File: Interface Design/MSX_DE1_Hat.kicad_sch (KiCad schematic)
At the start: 31 parts, among them J1 DE1 GPIO, J2 Conn_01x03_Male, J3 Conn_01x03_Male, J4 Conn_01x03_Male, J5 Conn_01x03_Male, J6 Conn_01x03_Male, J7 Conn_01x03_Male, J8 Conn_01x03_Male, U1 74LVC245A, U2 74LVC245A, U3 74LVC245A, U4 74LVC245A, U5 74LVC245A, U6 4077

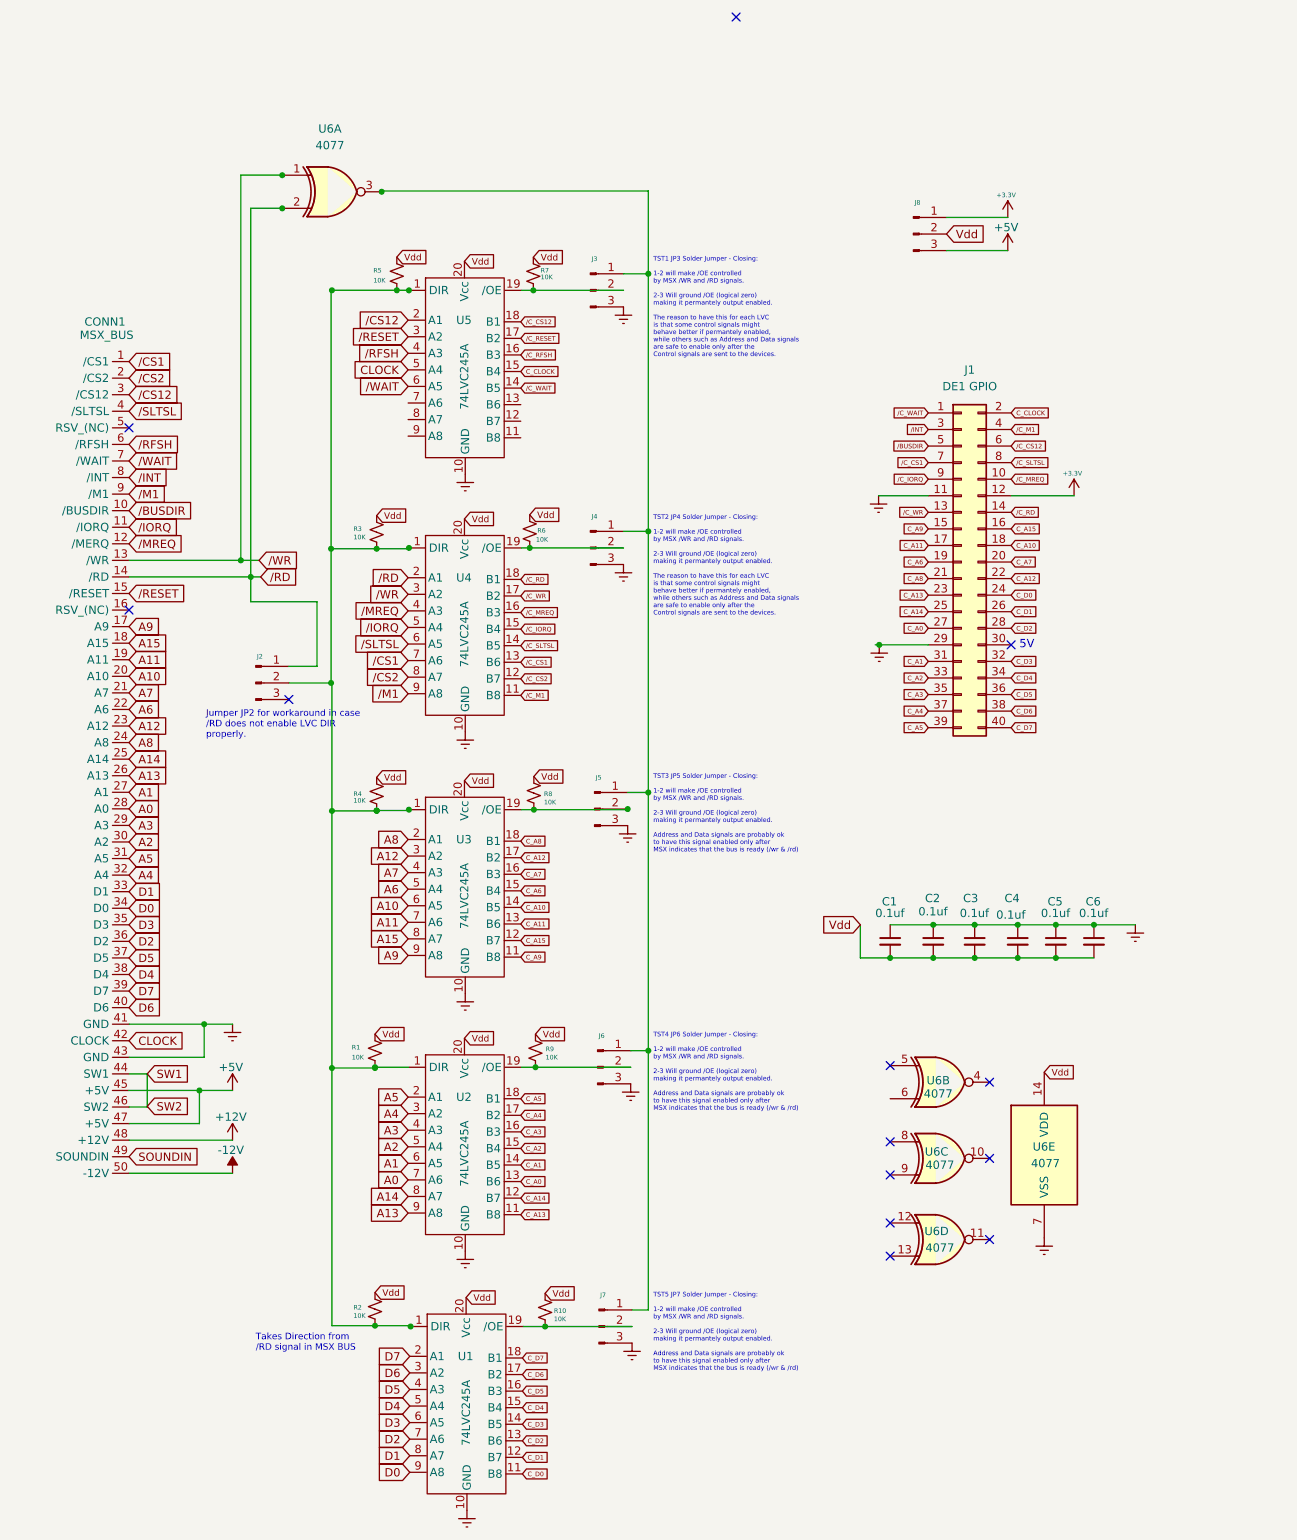
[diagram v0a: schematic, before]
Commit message: Added working firmware / vhdl. Updated schematic and pcb to rmove not needed components
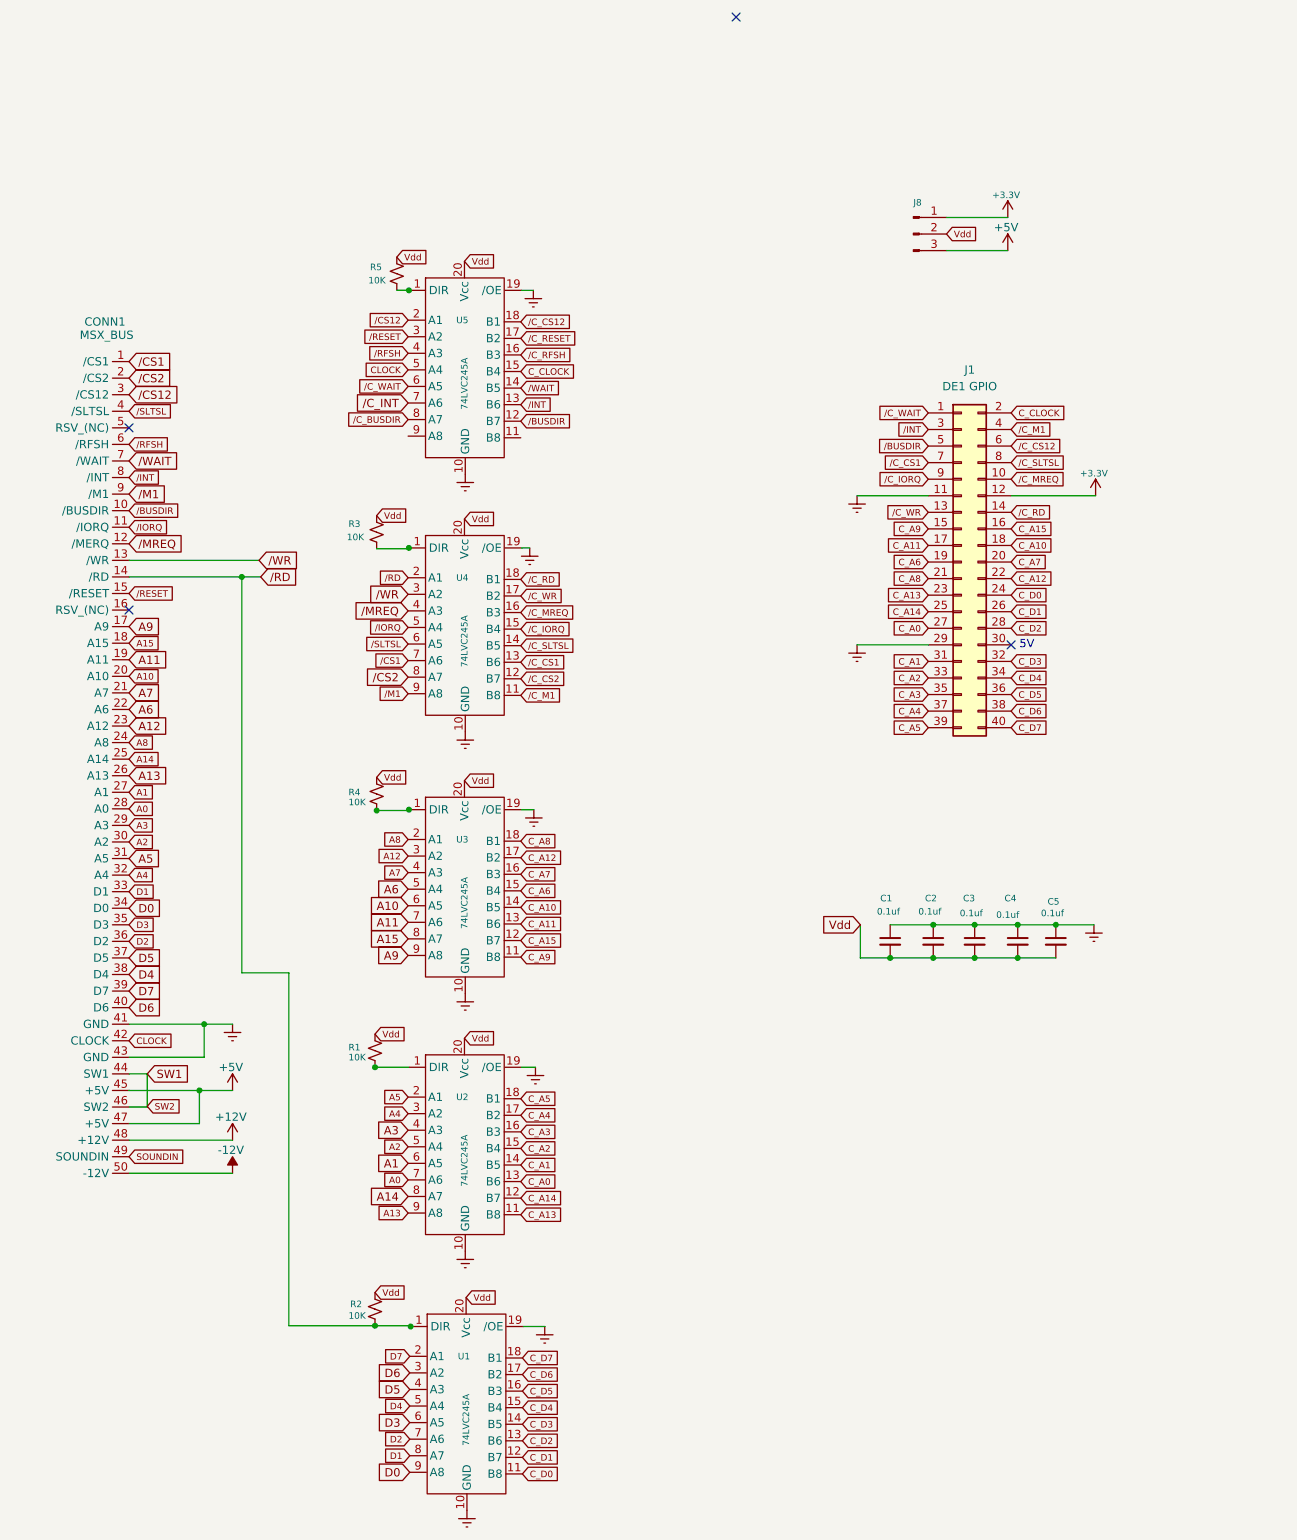
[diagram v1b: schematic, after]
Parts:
- removed C6: 0.1uf, Capacitor_THT:C_Disc_D3.0mm_W1.6mm_P2.50mm, symbol Device:C_Small
- removed J2, J3, J4, J5, J6, J7: Conn_01x03_Male, Connector_PinHeader_2.54mm:PinHeader_1x03_P2.54mm_Vertical, symbol Connector:Conn_01x03_Male
- removed R10, R6, R7, R8, R9: 10K, Resistor_THT:R_Axial_DIN0207_L6.3mm_D2.5mm_P7.62mm_Horizontal, symbol Device:R_Small_US
- removed U6: 4077, Package_DIP:DIP-14_W7.62mm, symbol 4xxx:4077
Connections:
- net GNDREF: now also U2.19 (/OE), U3.19 (/OE), U4.19 (/OE), U5.19 (/OE)
- net /BUSDIR: now also U5.12 (B7)
- net /C_WAIT: now also U5.6 (A5); no longer U5.14 (B5)
- net /INT: now also U5.13 (B6)
- net /RD: now also R2.2, U1.1 (DIR)
- net /WAIT: now also U5.14 (B5); no longer U5.6 (A5)
- net /C_INT: now reaches U5.7 (A6)
- net /C_BUSDIR: now reaches U5.8 (A7)
- new net: R4.2, U3.1 (DIR)
- new net: R1.2, U2.1 (DIR)
- new net: R3.2, U4.1 (DIR)
- new net: R5.2, U5.1 (DIR)
- no-connect marks 13 -> 4
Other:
- note removed: "Jumper JP2 for workaround in case /RD does not enable LVC DIR properly."
- note removed: "TST1 JP3 Solder Jumper - Closing: 1-2 will make /OE controlled by MSX /WR and /RD signals. 2-3 Will ground /OE (logical zero) making it permantely output enabled. The reason to have this for each LVC is that some control signals might behave better if permantely enabled, while others such as Address and Data signals are safe to enable only after the Control signals are sent to the devices."
- note removed: "TST2 JP4 Solder Jumper - Closing: 1-2 will make /OE controlled by MSX /WR and /RD signals. 2-3 Will ground /OE (logical zero) making it permantely output enabled. The reason to have this for each LVC is that some control signals might behave better if permantely enabled, while others such as Address and Data signals are safe to enable only after the Control signals are sent to the devices."
- note removed: "TST3 JP5 Solder Jumper - Closing: 1-2 will make /OE controlled by MSX /WR and /RD signals. 2-3 Will ground /OE (logical zero) making it permantely output enabled. Address and Data signals are probably ok to have this signal enabled only after MSX indicates that the bus is ready (/wr & /rd)"
- note removed: "TST4 JP6 Solder Jumper - Closing: 1-2 will make /OE controlled by MSX /WR and /RD signals. 2-3 Will ground /OE (logical zero) making it permantely output enabled. Address and Data signals are probably ok to have this signal enabled only after MSX indicates that the bus is ready (/wr & /rd)"
- note removed: "TST5 JP7 Solder Jumper - Closing: 1-2 will make /OE controlled by MSX /WR and /RD signals. 2-3 Will ground /OE (logical zero) making it permantely output enabled. Address and Data signals are probably ok to have this signal enabled only after MSX indicates that the bus is ready (/wr & /rd)"
- note removed: "Takes Direction from /RD signal in MSX BUS"

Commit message: Updated firmware and schematic following tests in Rev1.0 branch
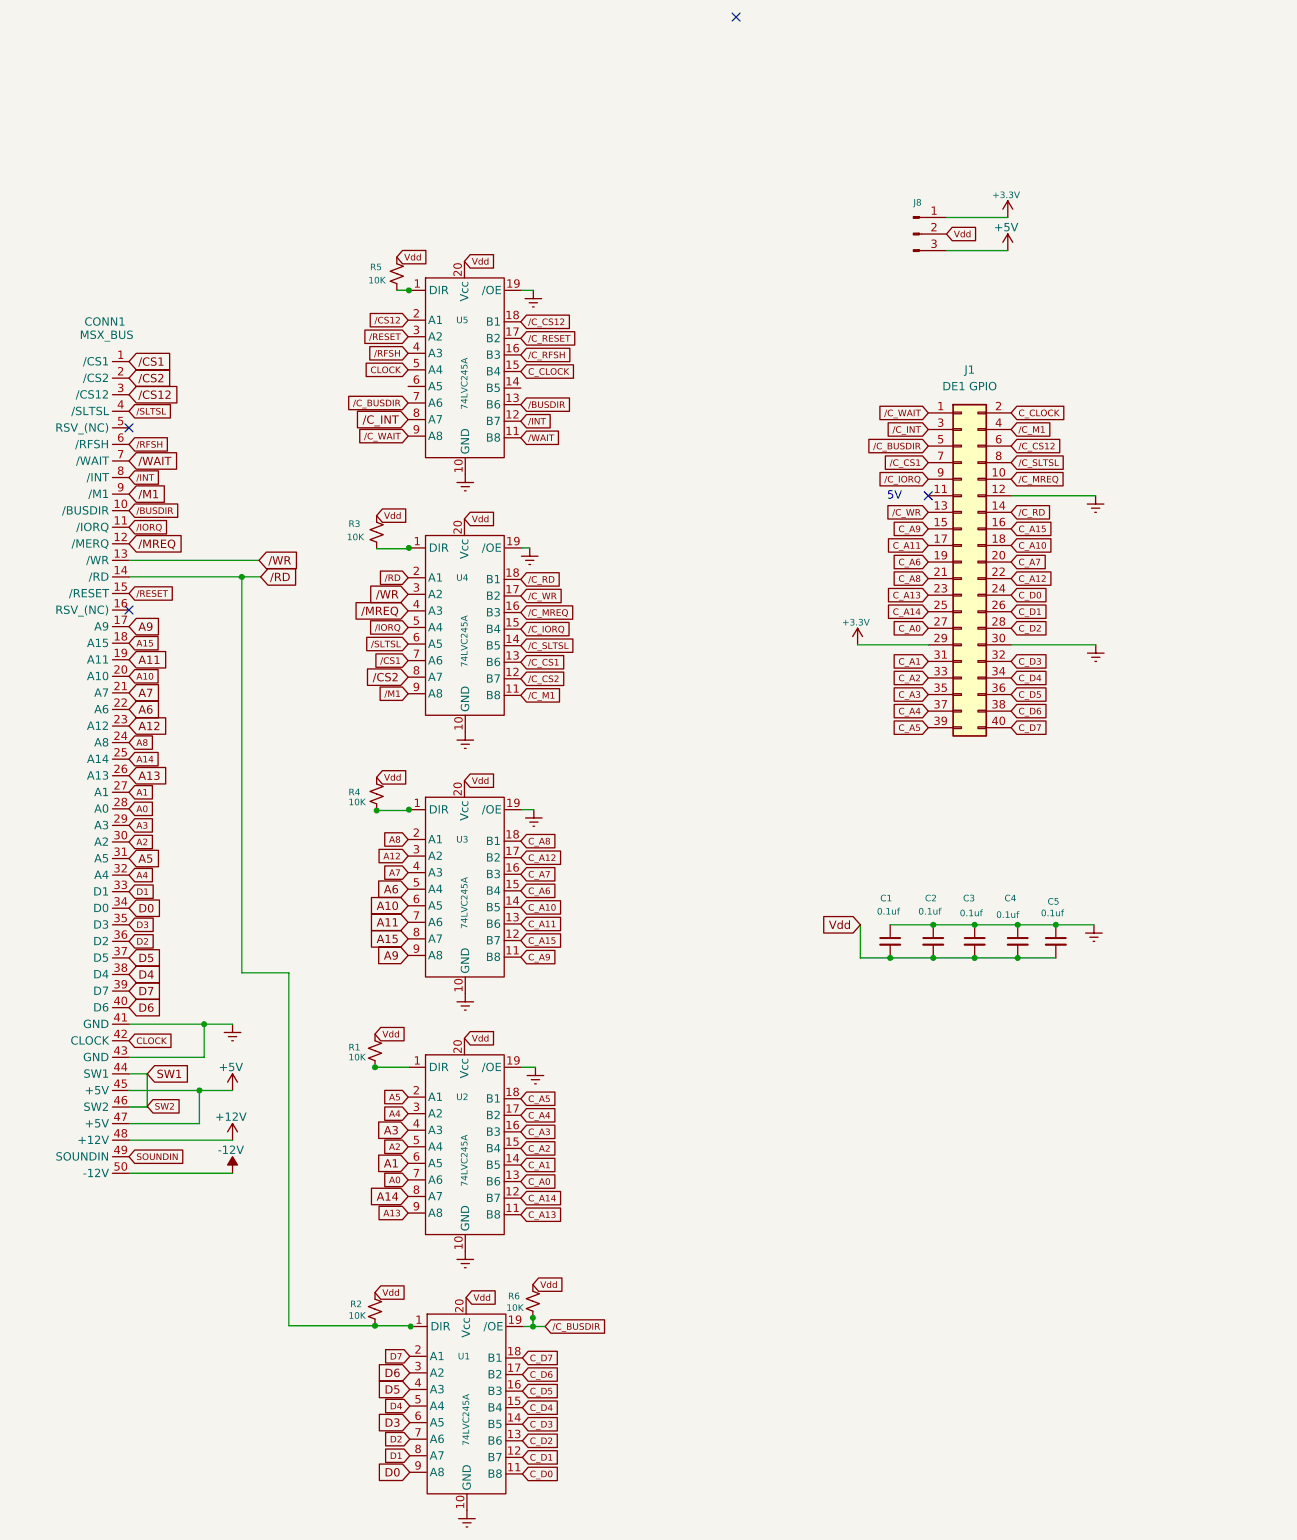
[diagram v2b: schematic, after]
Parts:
- added R6: 10K, Resistor_THT:R_Axial_DIN0207_L6.3mm_D2.5mm_P7.62mm_Horizontal, symbol Device:R_Small_US
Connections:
- net +3.3V: now also J1.29 (Pin_29); no longer J1.12 (Pin_12)
- net GNDREF: now also J1.12 (Pin_12), J1.30 (Pin_30); no longer J1.11 (Pin_11), J1.29 (Pin_29)
- net Vdd: now also R6.1
- net /BUSDIR: now also U5.13 (B6); no longer J1.5 (Pin_5), U5.12 (B7)
- net /C_BUSDIR: now also J1.5 (Pin_5), U1.19 (/OE), U5.7 (A6), R6.2; no longer U5.8 (A7)
- net /C_INT: now also J1.3 (Pin_3), U5.8 (A7); no longer U5.7 (A6)
- net /C_WAIT: now also U5.9 (A8); no longer U5.6 (A5)
- net /INT: now also U5.12 (B7); no longer J1.3 (Pin_3), U5.13 (B6)
- net /WAIT: now also U5.11 (B8); no longer U5.14 (B5)

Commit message: Starting routing of reivsed pcb
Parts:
- added J1: J1, Connector_PinHeader_2.54mm:PinHeader_1x03_P2.54mm_Vertical, symbol Connector:Conn_01x03_Male
- added J3: J3, Connector_PinHeader_2.54mm:PinHeader_1x02_P2.54mm_Vertical, symbol Connector_Generic:Conn_02x01
- added J4: J4, Connector_PinHeader_2.54mm:PinHeader_1x02_P2.54mm_Vertical, symbol Connector_Generic:Conn_02x01
- added J5: J5, Connector_PinHeader_2.54mm:PinHeader_1x02_P2.54mm_Vertical, symbol Connector_Generic:Conn_02x01
- added J6: J6, Connector_PinHeader_2.54mm:PinHeader_1x02_P2.54mm_Vertical, symbol Connector_Generic:Conn_02x01
- J2: renamed from J8; value Conn_01x03_Male -> J2
- renumbered J1 to IDC1
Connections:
- net +3.3V: now also C1.2, C2.2, C3.2, C4.2, C5.2, R1.1, R2.1, R3.1, R4.1, R5.1, R6.1, U1.20 (Vcc), U2.20 (Vcc), U3.20 (Vcc), U4.20 (Vcc), U5.20 (Vcc); no longer J2.1 (Pin_1)
- net +5V: no longer J2.3 (Pin_3)
- net C_CLOCK: now also J2.1 (Pin_1); no longer IDC1.2 (Pin_2)
- net /C_CS12: now also J1.3 (Pin_3); no longer IDC1.6 (Pin_6)
- net /C_CS2: now also J1.1 (Pin_1)
- net /C_RESET: now also J2.3 (Pin_3)
- net /C_RFSH: now also J4.2 (Pin_2); no longer U5.16 (B3)
- net /RFSH: now also J3.1 (Pin_1); no longer U5.4 (A3)
- net at U5.14 (B5): now also J6.1 (Pin_1)
- net at U5.6 (A5): now also J5.2 (Pin_2)
- removed net Vdd: C1.2, C2.2, C3.2, C4.2, C5.2, J2.2 (Pin_2), R1.1, R2.1, R3.1, R4.1, R5.1, R6.1, U1.20 (Vcc), U2.20 (Vcc), U3.20 (Vcc), U4.20 (Vcc), U5.20 (Vcc)
- new net: J4.1 (Pin_1), U5.16 (B3)
- new net: J3.2 (Pin_2), U5.4 (A3)
- new net C_CLK_OR_RST: IDC1.2 (Pin_2), J2.2 (Pin_2)
- new net C_CS2_CS12: IDC1.6 (Pin_6), J1.2 (Pin_2)
- no-connect marks 4 -> 5
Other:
- note added: "RFSH signal is trace nearby Input U5/In Pin 4/Out Pin 16. To use this signal, a GPIO pin will need to be re-wired to pin 16. J2: Use this jumper to choose to send CS2_n or CS12_n to IDC pin 6: 1-2: CS2_n 2-3: CS12_n J3: Use this jumper to choose to send CLOCK or RESET signal to IDC pin 2: 1-2: CLOCK 2-3: RESET J3&J4: Route RFSH to U5 pin4/pin16. Needs additional wiring to use this siganl, from J4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"
- moved on the sheet: C1, C2, C3, C4, C5, CONN1, IDC1, J2, R1, R2, R3, R4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
